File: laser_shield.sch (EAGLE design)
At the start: 36 parts, among them Q1 IRF3704S, Q2 IRF3704S, U1 ARDUINO_SHIELDLONGPADS

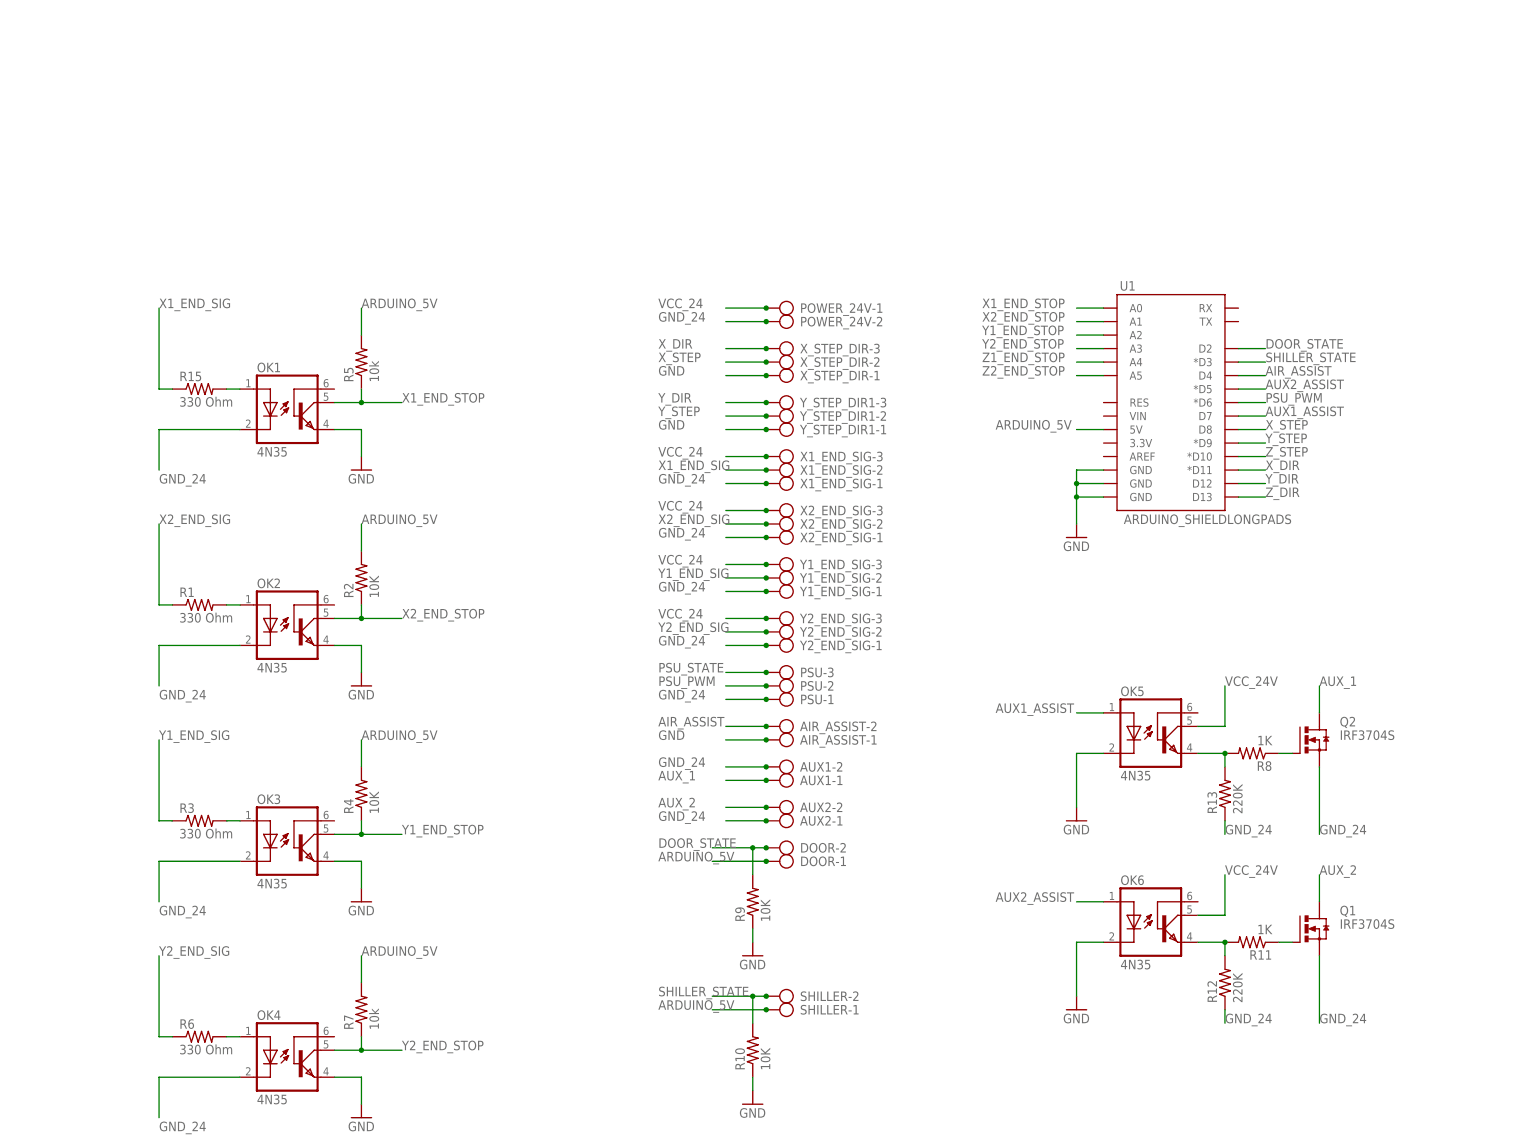
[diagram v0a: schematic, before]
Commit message: Modified for regular GRBL
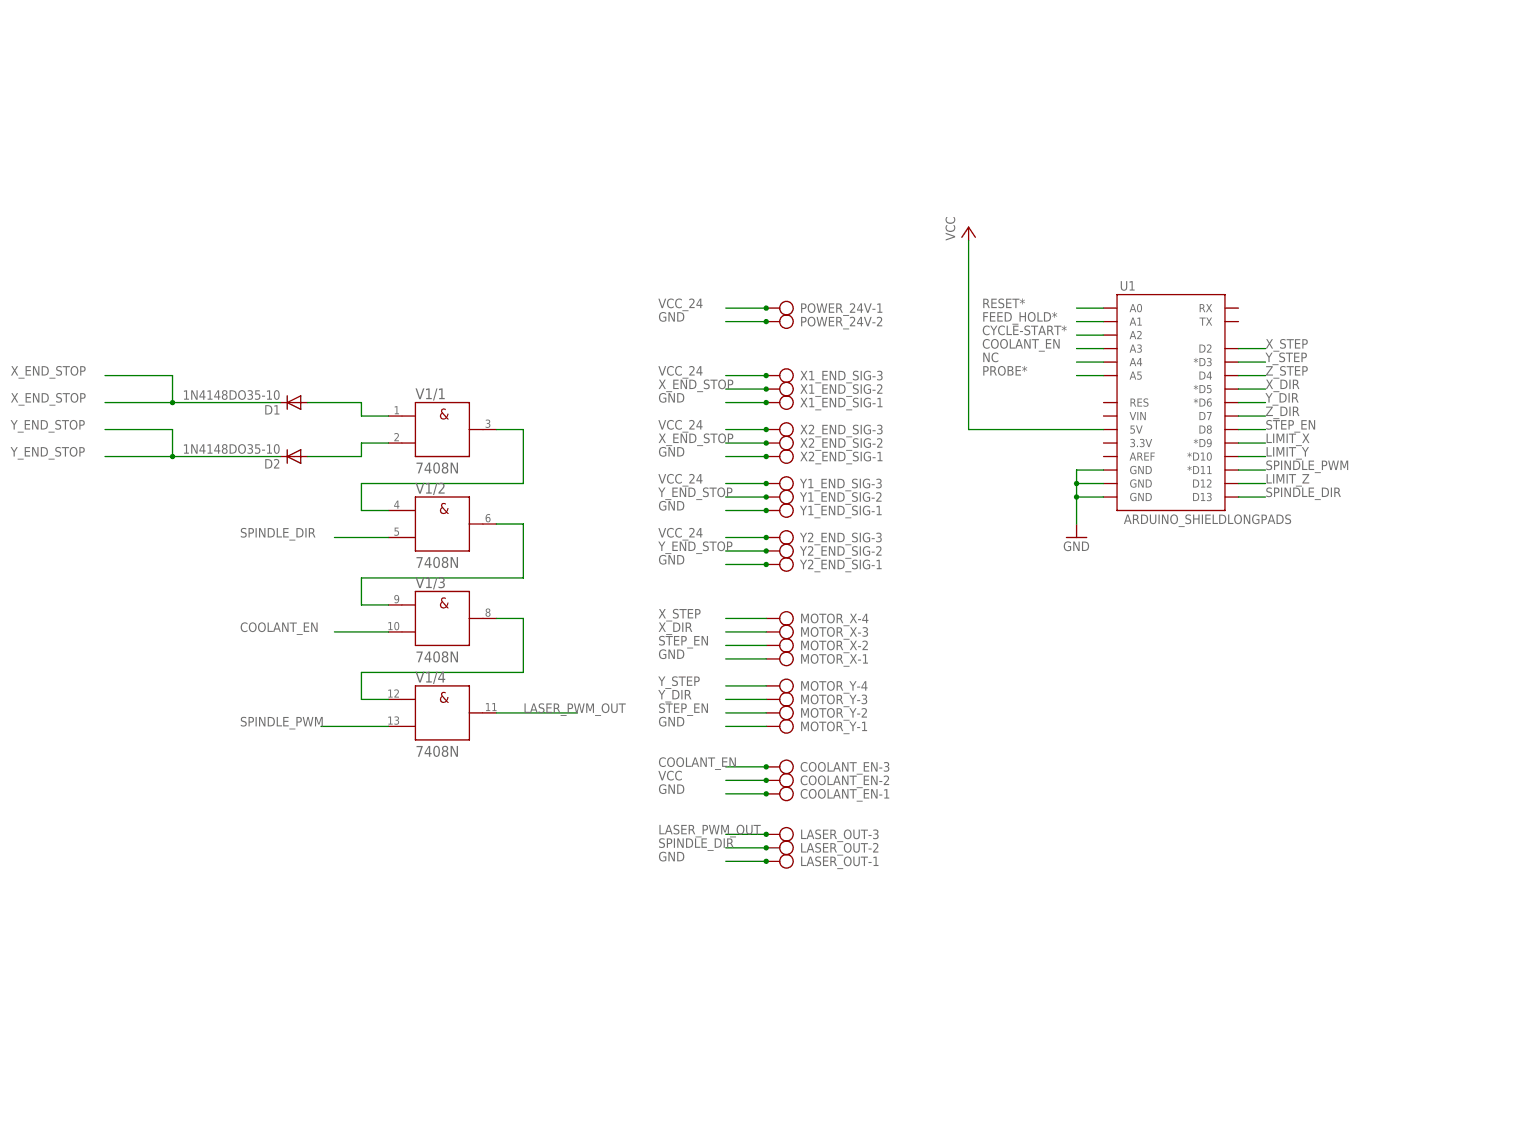
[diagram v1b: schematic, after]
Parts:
- removed AIR_ASSIST, AUX1, AUX2, DOOR, SHILLER: (no value), con-ptr500:AK300/2
- removed OK1, OK2, OK3, OK4, OK5, OK6: 4N35, optocoupler:4N35
- removed PSU, X_STEP_DIR, Y_STEP_DIR1: (no value), con-ptr500:AK300/3
- removed Q1, Q2: IRF3704S, transistor-power:IRF3704S
- removed R1, R15, R3, R6: 330 Ohm, rcl:R-US_0207/7
- removed R10, R2, R4, R9: 10K, rcl:R-US_0207/7
- removed R11, R8: 1K, rcl:R-US_0207/7
- removed R12, R13: 220K, rcl:R-US_0207/7
- removed R5, R7: 10k, rcl:R-US_0207/7
- added COOLANT_EN, LASER_OUT: (no value), con-ptr500:AK300/3
- added D1, D2: 1N4148DO35-10, diode:1N4148DO35-10
- added MOTOR_X, MOTOR_Y: (no value), con-ptr500:AK300/4
- added V1: 7408N, 74ttl-din:7408N
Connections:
- net Z1_END_STOP renamed NC
- net Z2_END_STOP renamed PROBE*
- removed net AIR_ASSIST: AIR_ASSIST-2.KL, U1.D4
- removed net ARDUINO_5V: DOOR-1.KL, R2.2, R4.2, R5.2, R7.2, SHILLER-1.KL, U1.5V
- removed net AUX1_ASSIST: OK5.A, U1.D7
- removed net AUX2_ASSIST: OK6.A, U1.*D5
- removed net AUX_1: AUX1-1.KL, Q2.D
- removed net AUX_2: AUX2-2.KL, Q1.D
- removed net DOOR_STATE: DOOR-2.KL, R9.2, U1.D2
- removed net GND_24: AUX1-2.KL, AUX2-1.KL, OK1.C, OK2.C, OK3.C, OK4.C, POWER_24V-2.KL, PSU-1.KL, Q1.S, Q2.S, R12.1, R13.1, X1_END_SIG-1.KL, X2_END_SIG-1.KL, Y1_END_SIG-1.KL, Y2_END_SIG-1.KL
- removed net N$6: OK5.EMI, R13.2, R8.2
- removed net N$8: Q1.G, R11.1
- removed net N$9: OK6.EMI, R11.2, R12.2
- removed net PSU_PWM: PSU-2.KL, U1.*D6
- removed net PSU_STATE: PSU-3.KL
- removed net SHILLER_STATE: R10.2, SHILLER-2.KL, U1.*D3
- removed net VCC_24V: OK5.COL, OK6.COL
- removed net X1_END_SIG: R15.1, X1_END_SIG-2.KL
- removed net X1_END_STOP: OK1.COL, R5.1, U1.A0
- removed net X2_END_SIG: R1.1, X2_END_SIG-2.KL
- removed net X2_END_STOP: OK2.COL, R2.1, U1.A1
- removed net Y1_END_SIG: R3.1, Y1_END_SIG-2.KL
- removed net Y1_END_STOP: OK3.COL, R4.1, U1.A2
- removed net Y2_END_SIG: R6.1, Y2_END_SIG-2.KL
- removed net Y2_END_STOP: OK4.COL, R7.1, U1.A3
- new net COOLANT_EN: COOLANT_EN-3.KL, U1.A3, V1/3.B
- new net CYCLE-START*: U1.A2
- new net FEED_HOLD*: U1.A1
- new net LASER_PWM_OUT: LASER_OUT-3.KL, V1/4.Y
- new net LIMIT_X: U1.*D9
- new net LIMIT_Y: U1.*D10
- new net LIMIT_Z: U1.D12
- new net RESET*: U1.A0
- new net SPINDLE_DIR: LASER_OUT-2.KL, U1.D13, V1/2.B
- new net SPINDLE_PWM: U1.*D11, V1/4.B
- new net STEP_EN: MOTOR_X-2.KL, MOTOR_Y-2.KL, U1.D8
- new net VCC: COOLANT_EN-2.KL, U1.5V
- new net X_END_STOP: D1.C, X1_END_SIG-2.KL, X2_END_SIG-2.KL
- new net Y_END_STOP: D2.C, Y1_END_SIG-2.KL, Y2_END_SIG-2.KL
- net GND: now also COOLANT_EN-1.KL, LASER_OUT-1.KL, MOTOR_X-1.KL, MOTOR_Y-1.KL, POWER_24V-2.KL, X1_END_SIG-1.KL, X2_END_SIG-1.KL, Y1_END_SIG-1.KL, Y2_END_SIG-1.KL; no longer AIR_ASSIST-1.KL, OK1.EMI, OK2.EMI, OK3.EMI, OK4.EMI, OK5.C, OK6.C, R10.1, R9.1, X_STEP_DIR-1.KL, Y_STEP_DIR1-1.KL
- net N$1: now also D1.A, V1/1.A; no longer OK2.A, R1.2
- net N$2: now also D2.A, V1/1.B; no longer OK3.A, R3.2
- net N$3: now also V1/1.Y, V1/2.A; no longer OK4.A, R6.2
- net N$4: now also V1/2.Y, V1/3.A; no longer Q2.G, R8.1
- net N$5: now also V1/3.Y, V1/4.A; no longer OK1.A, R15.2
- net X_DIR: now also MOTOR_X-3.KL, U1.*D5; no longer U1.*D11, X_STEP_DIR-3.KL
- net X_STEP: now also MOTOR_X-4.KL, U1.D2; no longer U1.D8, X_STEP_DIR-2.KL
- net Y_DIR: now also MOTOR_Y-3.KL, U1.*D6; no longer U1.D12, Y_STEP_DIR1-3.KL
- net Y_STEP: now also MOTOR_Y-4.KL, U1.*D3; no longer U1.*D9, Y_STEP_DIR1-2.KL
- net Z_DIR: now also U1.D7; no longer U1.D13
- net Z_STEP: now also U1.D4; no longer U1.*D10
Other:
- moved on the sheet: X1_END_SIG-1, X1_END_SIG-2, X1_END_SIG-3, X2_END_SIG-1, X2_END_SIG-2, X2_END_SIG-3, Y1_END_SIG-1, Y1_END_SIG-2, Y1_END_SIG-3, Y2_END_SIG-1, Y2_END_SIG-2, Y2_END_SIG-3

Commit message: Added new connectors
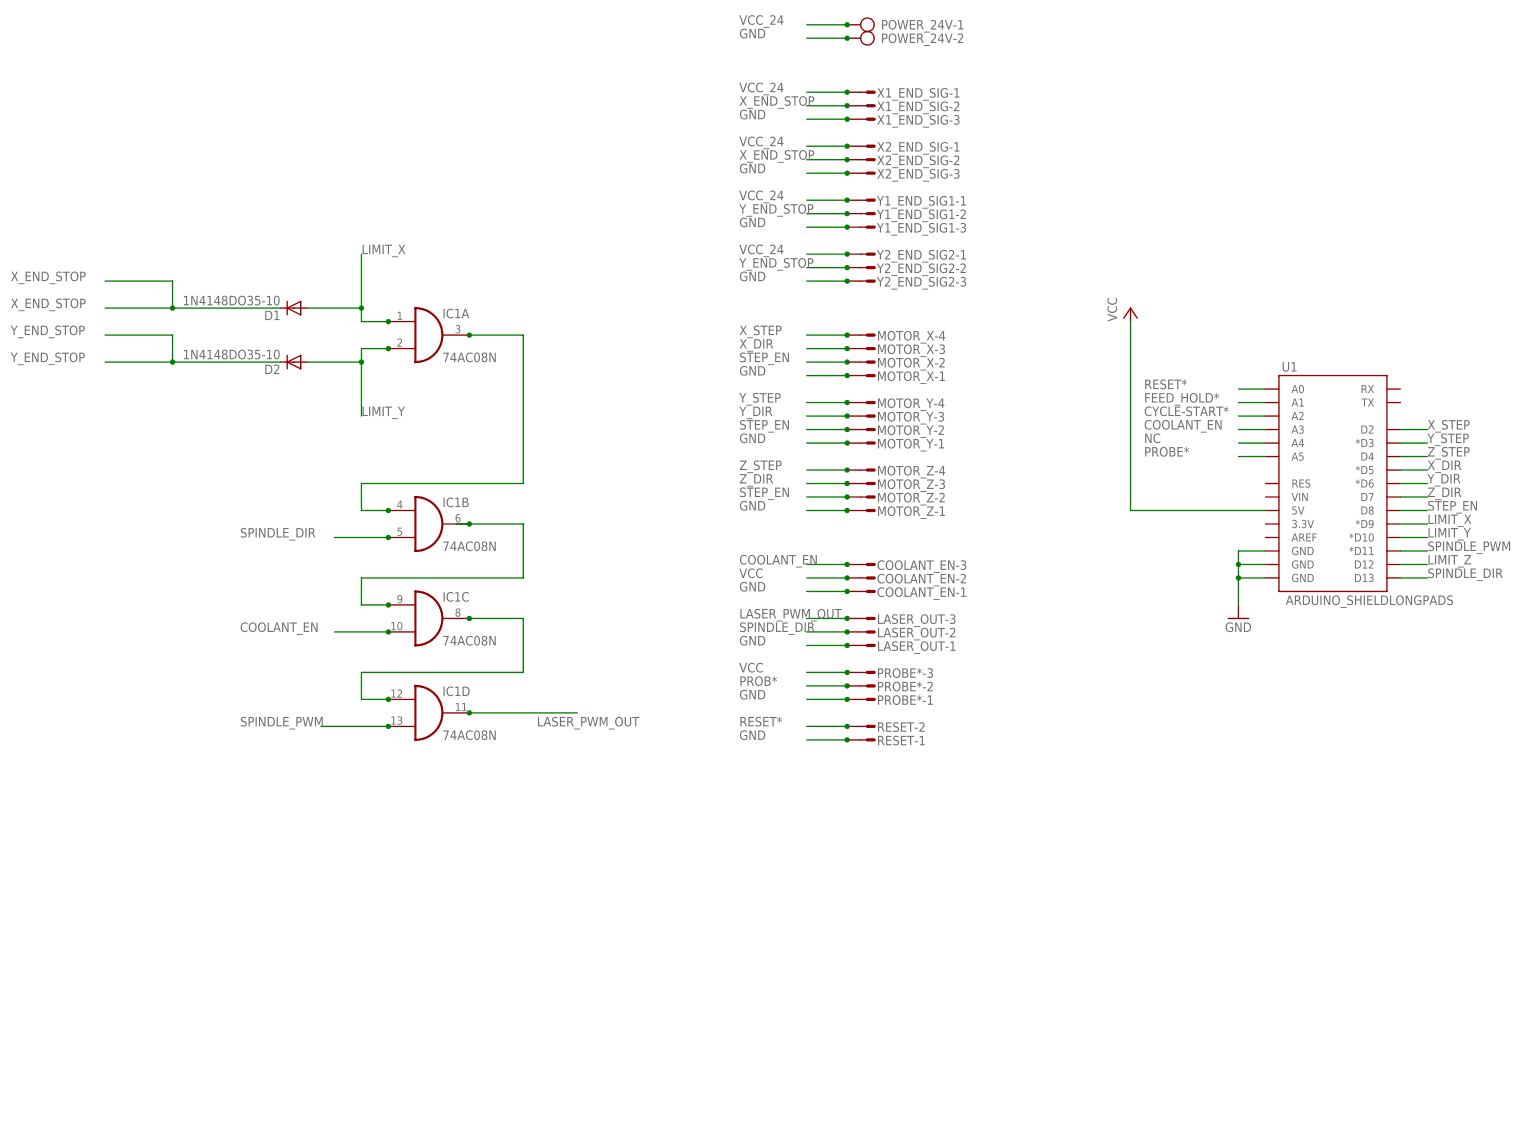
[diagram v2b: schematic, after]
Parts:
- removed V1: 7408N, 74ttl-din:7408N
- removed Y1_END_SIG, Y2_END_SIG: (no value), con-ptr500:AK300/3
- added IC1: 74AC08N, 74xx-eu:74AC08N
- added MOTOR_Z: (no value), con-amp-mt:L04P
- added PROBE*, Y1_END_SIG1, Y2_END_SIG2: (no value), con-amp-mt:L03P
- added RESET: (no value), con-amp-mt:L02P
- COOLANT_EN, LASER_OUT, X1_END_SIG, X2_END_SIG: device con-ptr500:AK300/3 -> con-amp-mt:L03P
- MOTOR_X, MOTOR_Y: device con-ptr500:AK300/4 -> con-amp-mt:L04P
- POWER_24V: device con-ptr500:AK500/2-H -> con-ptr500:AK300/2
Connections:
- removed net N$1: D1.A, V1/1.A
- removed net N$2: D2.A, V1/1.B
- new net PROB*: PROBE*-2.S
- net COOLANT_EN: now also COOLANT_EN-3.S, IC1C.I1; no longer COOLANT_EN-3.KL, V1/3.B
- net GND: now also COOLANT_EN-1.S, LASER_OUT-1.S, MOTOR_X-1.S, MOTOR_Y-1.S, MOTOR_Z-1.S, PROBE*-1.S, RESET-1.S, X1_END_SIG-3.S, X2_END_SIG-3.S, Y1_END_SIG1-3.S, Y2_END_SIG2-3.S; no longer COOLANT_EN-1.KL, LASER_OUT-1.KL, MOTOR_X-1.KL, MOTOR_Y-1.KL, X1_END_SIG-1.KL, X2_END_SIG-1.KL, Y1_END_SIG-1.KL, Y2_END_SIG-1.KL
- net LASER_PWM_OUT: now also IC1D.O, LASER_OUT-3.S; no longer LASER_OUT-3.KL, V1/4.Y
- net LIMIT_X: now also D1.A, IC1A.I0
- net LIMIT_Y: now also D2.A, IC1A.I1
- net N$3: now also IC1A.O, IC1B.I0; no longer V1/1.Y, V1/2.A
- net N$4: now also IC1B.O, IC1C.I0; no longer V1/2.Y, V1/3.A
- net N$5: now also IC1C.O, IC1D.I0; no longer V1/3.Y, V1/4.A
- net RESET*: now also RESET-2.S
- net SPINDLE_DIR: now also IC1B.I1, LASER_OUT-2.S; no longer LASER_OUT-2.KL, V1/2.B
- net SPINDLE_PWM: now also IC1D.I1; no longer V1/4.B
- net STEP_EN: now also MOTOR_X-2.S, MOTOR_Y-2.S, MOTOR_Z-2.S; no longer MOTOR_X-2.KL, MOTOR_Y-2.KL
- net VCC: now also COOLANT_EN-2.S, PROBE*-3.S; no longer COOLANT_EN-2.KL
- net VCC_24: now also X1_END_SIG-1.S, X2_END_SIG-1.S, Y1_END_SIG1-1.S, Y2_END_SIG2-1.S; no longer X1_END_SIG-3.KL, X2_END_SIG-3.KL, Y1_END_SIG-3.KL, Y2_END_SIG-3.KL
- net X_DIR: now also MOTOR_X-3.S; no longer MOTOR_X-3.KL
- net X_END_STOP: now also X1_END_SIG-2.S, X2_END_SIG-2.S; no longer X1_END_SIG-2.KL, X2_END_SIG-2.KL
- net X_STEP: now also MOTOR_X-4.S; no longer MOTOR_X-4.KL
- net Y_DIR: now also MOTOR_Y-3.S; no longer MOTOR_Y-3.KL
- net Y_END_STOP: now also Y1_END_SIG1-2.S, Y2_END_SIG2-2.S; no longer Y1_END_SIG-2.KL, Y2_END_SIG-2.KL
- net Y_STEP: now also MOTOR_Y-4.S; no longer MOTOR_Y-4.KL
- net Z_DIR: now also MOTOR_Z-3.S
- net Z_STEP: now also MOTOR_Z-4.S
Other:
- moved on the sheet: D1, D2, POWER_24V-1, POWER_24V-2, U1

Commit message: New rooting
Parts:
- added CYCLE_S, FEED_H: (no value), con-amp-mt:L02P
- renumbered PROBE* to PROBE
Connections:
- removed net CYCLE-START*: U1.A2
- removed net PROB*: PROBE-2.S
- new net CYCLE_START*: CYCLE_S-2.S, U1.A2
- net FEED_HOLD*: now also FEED_H-2.S
- net GND: now also CYCLE_S-1.S, FEED_H-1.S
- net PROBE*: now also PROBE-2.S
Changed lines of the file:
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@@
 </variantdefs>
 <classes>
-<class number="0" name="default" width="0" drill="0">
+<class number="0" name="default" width="0.0254" drill="0.8">
+<clearance class="0" value="0.0254"/>
 </class>
-<class number="2" name="gnd_plane" width="2" drill="0.8">
+<class number="2" name="VCC_24" width="1" drill="0.8">
 <clearance class="2" value="0.0254"/>
 </class>
@@
 <part name="X1_END_SIG" library="con-amp-mt" deviceset="L03P" device=""/>
 <part name="IC1" library="74xx-eu" deviceset="74*08" device="N" technology="AC"/>
-<part name="PROBE*" library="con-amp-mt" deviceset="L03P" device=""/>
+<part name="PROBE" library="con-amp-mt" deviceset="L03P" device=""/>
 <part name="Y1_END_SIG1" library="con-amp-mt" deviceset="L03P" device=""/>
 <part name="Y2_END_SIG2" library="con-amp-mt" deviceset="L03P" device=""/>
 <part name="MOTOR_Z" library="con-amp-mt" deviceset="L04P" device=""/>
+<part name="FEED_H" library="con-amp-mt" deviceset="L02P" device=""/>
+<part name="CYCLE_S" library="con-amp-mt" deviceset="L02P" device=""/>
 </parts>
 <sheets>
@@
 <instance part="IC1" gate="C" x="-20.32" y="12.7"/>
 <instance part="IC1" gate="D" x="-20.32" y="-5.08"/>
-<instance part="PROBE*" gate="-1" x="63.5" y="-2.54" rot="R180"/>
-<instance part="PROBE*" gate="-2" x="63.5" y="0" rot="R180"/>
-<instance part="PROBE*" gate="-3" x="63.5" y="2.54" rot="R180"/>
+<instance part="PROBE" gate="-1" x="63.5" y="-2.54" rot="R180"/>
+<instance part="PROBE" gate="-2" x="63.5" y="0" rot="R180"/>
+<instance part="PROBE" gate="-3" x="63.5" y="2.54" rot="R180"/>
 <instance part="Y1_END_SIG1" gate="-1" x="63.5" y="91.44" rot="R180"/>
 <instance part="Y1_END_SIG1" gate="-2" x="63.5" y="88.9" rot="R180"/>
@@
 <instance part="MOTOR_Z" gate="-3" x="63.5" y="38.1" rot="R180"/>
 <instance part="MOTOR_Z" gate="-4" x="63.5" y="40.64" rot="R180"/>
+<instance part="FEED_H" gate="-1" x="63.5" y="-17.78" rot="R180"/>
+<instance part="FEED_H" gate="-2" x="63.5" y="-15.24" rot="R180"/>
+<instance part="CYCLE_S" gate="-1" x="63.5" y="-25.4" rot="R180"/>
+<instance part="CYCLE_S" gate="-2" x="63.5" y="-22.86" rot="R180"/>
 </instances>
 <busses>
@@
 <segment>
 <wire x1="58.42" y1="-2.54" x2="50.8" y2="-2.54" width="0.1524" layer="91"/>
-<pinref part="PROBE*" gate="-1" pin="S"/>
+<pinref part="PROBE" gate="-1" pin="S"/>
 <junction x="58.42" y="-2.54"/>
 <label x="38.1" y="-2.54" size="1.778" layer="95"/>
@@
 <junction x="58.42" y="33.02"/>
 </segment>
+<segment>
+<pinref part="FEED_H" gate="-1" pin="S"/>
+<wire x1="58.42" y1="-17.78" x2="50.8" y2="-17.78" width="0.1524" layer="91"/>
+<label x="38.1" y="-17.78" size="1.778" layer="95"/>
+<junction x="58.42" y="-17.78"/>
+</segment>
+<segment>
+<pinref part="CYCLE_S" gate="-1" pin="S"/>
+<wire x1="58.42" y1="-25.4" x2="50.8" y2="-25.4" width="0.1524" layer="91"/>
+<label x="38.1" y="-25.4" size="1.778" layer="95"/>
+<junction x="58.42" y="-25.4"/>
+</segment>
 </net>
 <net name="X_STEP" class="0">
@@
 <label x="114.3" y="43.18" size="1.778" layer="95"/>
 </segment>
+<segment>
+<wire x1="58.42" y1="0" x2="50.8" y2="0" width="0.1524" layer="91"/>
+<pinref part="PROBE" gate="-2" pin="S"/>
+<junction x="58.42" y="0"/>
+<label x="38.1" y="0" size="1.778" layer="95"/>
+</segment>
 </net>
 <net name="NC" class="0">
@@
 </segment>
 </net>
-<net name="VCC_24" class="0">
+<net name="VCC_24" class="2">
 <segment>
 <wire x1="58.42" y1="124.46" x2="50.8" y2="124.46" width="0.1524" layer="91"/>
@@
 <segment>
 <wire x1="58.42" y1="2.54" x2="50.8" y2="2.54" width="0.1524" layer="91"/>
-<pinref part="PROBE*" gate="-3" pin="S"/>
+<pinref part="PROBE" gate="-3" pin="S"/>
 <junction x="58.42" y="2.54"/>
 <label x="38.1" y="2.54" size="1.778" layer="95"/>
@@
 <label x="114.3" y="53.34" size="1.778" layer="95"/>
 </segment>
-</net>
-<net name="CYCLE-START*" class="0">
-<segment>
-<pinref part="U1" gate="G$1" pin="A2"/>
-<wire x1="137.16" y1="50.8" x2="132.08" y2="50.8" width="0.1524" layer="91"/>
-<label x="114.3" y="50.8" size="1.778" layer="95"/>
+<segment>
+<pinref part="FEED_H" gate="-2" pin="S"/>
+<wire x1="58.42" y1="-15.24" x2="50.8" y2="-15.24" width="0.1524" layer="91"/>
+<label x="38.1" y="-15.24" size="1.778" layer="95"/>
+<junction x="58.42" y="-15.24"/>
 </segment>
 </net>
@@
 </segment>
 </net>
-<net name="PROB*" class="0">
-<segment>
-<wire x1="58.42" y1="0" x2="50.8" y2="0" width="0.1524" layer="91"/>
-<pinref part="PROBE*" gate="-2" pin="S"/>
-<junction x="58.42" y="0"/>
-<label x="38.1" y="0" size="1.778" layer="95"/>
-</segment>
-</net>
+<net name="CYCLE_START*" class="0">
+<segment>
+<pinref part="CYCLE_S" gate="-2" pin="S"/>
+<wire x1="58.42" y1="-22.86" x2="50.8" y2="-22.86" width="0.1524" layer="91"/>
+<label x="38.1" y="-22.86" size="1.778" layer="95"/>
+<junction x="58.42" y="-22.86"/>
+</segment>
+<segment>
+<pinref part="U1" gate="G$1" pin="A2"/>
+<wire x1="137.16" y1="50.8" x2="132.08" y2="50.8" width="0.1524" layer="91"/>
+<label x="114.3" y="50.8" size="1.778" layer="95"/>
+</segment>
+</net>
